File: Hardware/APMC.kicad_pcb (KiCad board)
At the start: 2 copper layers, 85 x 52.5 mm, 148 parts, among them J1 Pin header Male 2x7 P:1.27, J10 Conn_01x03, J11 Conn_01x03, J12 Conn_02x08, J13 Conn_01x03, J14 Conn_01x04, J2 USB-C receptacle, J5 Terminal 1x5 P:3.5mm, J6 Terminal 1x5 P:3.5mm, J7 Terminal 1x5 P:3.5mm, J8 Conn_01x04, J9 Conn_01x04, M1 Logo_Open_Hardware_Small, Q1 DMP6023LE, Q2 DMP6023LE, Q3 DMP6023LE, Q4 BSS123, Q5 DMP6023LE, Q6 DMP6023LE, Q7 BSS123, Q8 DMP3056L, U1 LMR51610, U10 TXU0202, U11 PCA9306, U12 LM74703/LM74704, U13 TPS62162DSG, U2 LCFE201202A, U3 TXU0202, U4 M95P32, U5 STM32U575CITx, U6 XTR200, U7 TPS7A2031PDBVR, U8 XTR200, U9 ADS1x2S14, X1 SiT8008Bx-7x, Y1 32.768kHz

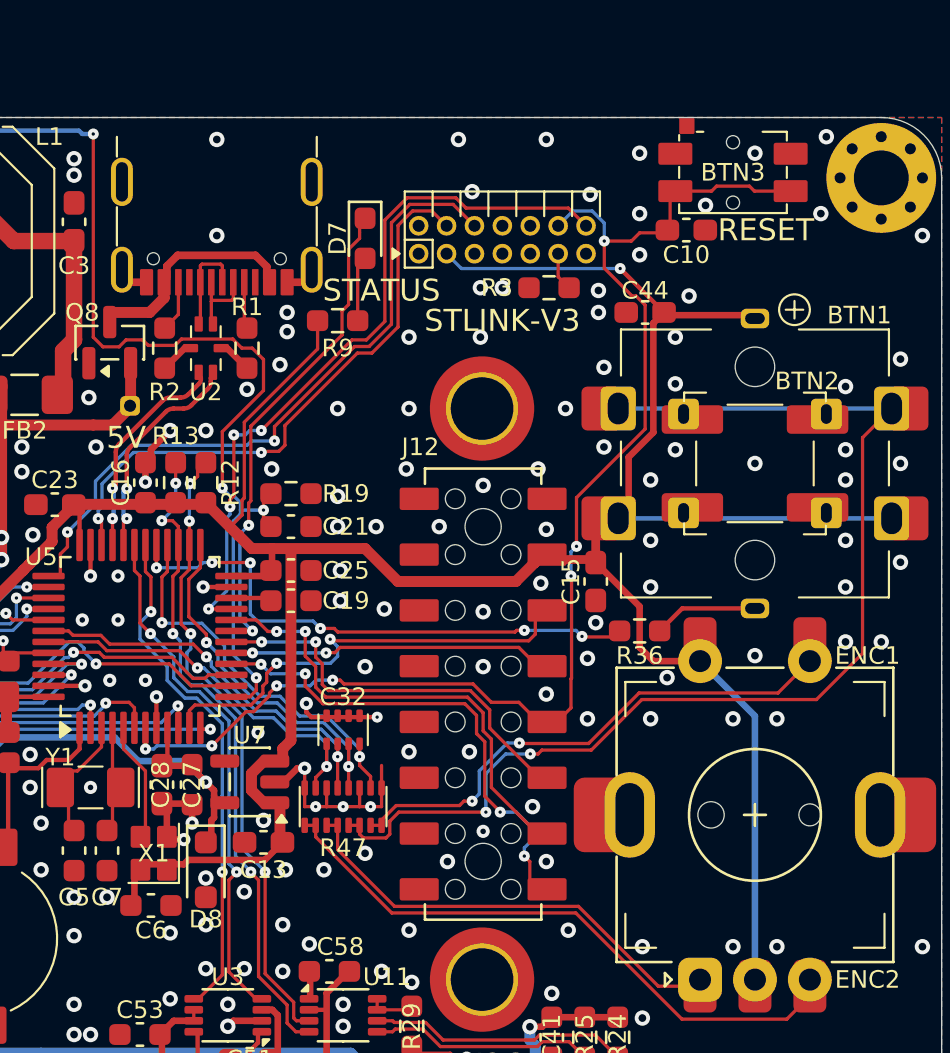
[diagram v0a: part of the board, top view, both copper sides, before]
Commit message: LCD pin header modified
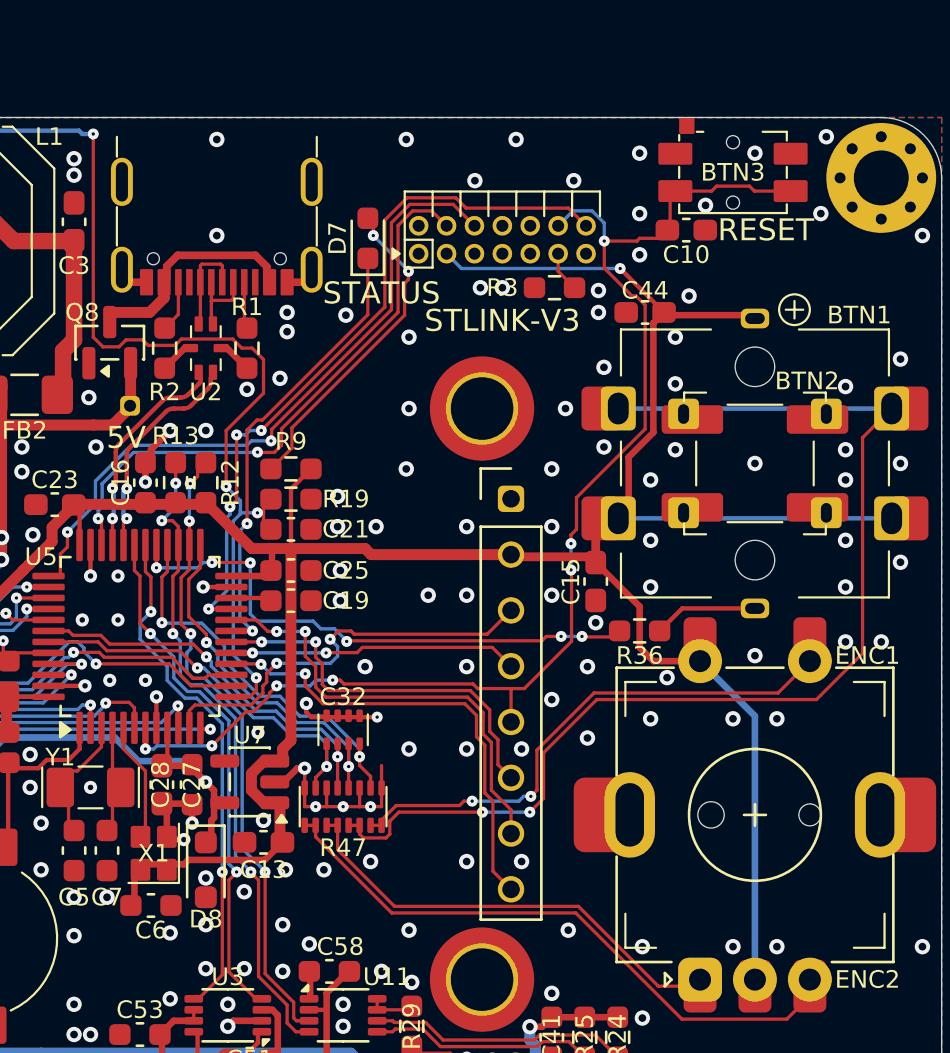
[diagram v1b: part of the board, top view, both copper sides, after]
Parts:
- J12: value Conn_02x08 -> Conn_01x08; footprint Custom:Harwin_M20-7810845_2x08_P2.54mm_Vertical -> Custom:PinHeader_1x08_P2.54mm_Vertical
- moved R9 7.08 mm to (82.9, 29.0), turned to 0 degrees
- moved J12 1.27 mm to (92.9, 39.2)
- moved R19 0.25 mm to (82.9, 30.4)
- moved R3 0.25 mm to (94.9, 20.8)
- moved C21 0.12 mm to (82.9, 31.8)
- moved D7 0.12 mm to (86.4, 18.5), turned to 90 degrees
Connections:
- J12 pad 1: unconnected-(J12-Pin_1-Pad1) -> GND
- J12 pad 2: GND -> /VDD
- J12 pad 3: unconnected-(J12-Pin_3-Pad3) -> /LCD_SCK
- J12 pad 4: /VDD -> /LCD_MOSI
- J12 pad 5: unconnected-(J12-Pin_5-Pad5) -> /NRST
- J12 pad 6: /LCD_SCK -> /LCD_DC
- J12 pad 7: unconnected-(J12-Pin_7-Pad7) -> /LCD_CS
- J12 pad 8: /LCD_MOSI -> /LCD_PWM
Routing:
- net Net-(D7-A): track 2.98 -> 14.9 mm, vias 0 -> 2
- net /VDD: track 284.5 -> 277.4 mm
- net /LCD_SCK: track 20.5 -> 18.9 mm
- net /STATUS_LED: track 22.2 -> 20.7 mm
- net /NRST: track 59.5 -> 58.4 mm
- net /LCD_PWM: track 22.0 -> 21.0 mm, vias 4 -> 2
- net /LCD_MOSI: track 14.3 -> 13.3 mm
- net /ADC0: track 63.0 -> 63.9 mm
- net GND: vias 328 -> 324

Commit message: PCB refined
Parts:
- moved R9 10.6 mm to (89.5, 20.8)
- moved BT1 4.12 mm to (72.8, 50.4)
- moved R6 3.51 mm to (68.9, 43.4)
- moved C13 3.50 mm to (85.1, 46.0)
- moved C16 3.50 mm to (79.8, 29.6)
- moved C19 3.50 mm to (86.4, 35.0)
- moved C21 3.50 mm to (86.4, 31.8)
- moved C22 3.50 mm to (72.6, 42.4)
- moved C23 3.50 mm to (75.6, 30.6)
- moved C24 3.50 mm to (72.6, 41.0)
- moved C25 3.50 mm to (86.4, 33.6)
- moved C26 3.50 mm to (72.4, 39.4)
- moved C27 3.50 mm to (80.5, 43.4)
- moved C28 3.50 mm to (81.9, 43.4)
- moved C32 3.50 mm to (88.8, 40.9)
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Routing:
- net Net-(D7-A): track 14.9 -> 4.20 mm
- net /C: track 24.3 -> 17.8 mm
- net /5V: track 104.3 -> 99.5 mm
- net /NRST: track 58.4 -> 53.8 mm
- net /A: track 20.7 -> 16.8 mm
- net /D: track 53.1 -> 49.4 mm
- net /LCD_DC: track 17.5 -> 14.0 mm
- net /LCD_PWM: track 21.0 -> 17.5 mm
- net /LCD_MOSI: track 13.3 -> 9.82 mm
- net /LCD_CS: track 20.4 -> 16.9 mm
- net /LCD_SCK: track 18.9 -> 15.4 mm
- net /PWM0: track 24.9 -> 21.7 mm
- net /EF2: track 38.7 -> 41.7 mm
- net /PWM2: track 31.9 -> 34.9 mm
- net /PWM1: track 32.4 -> 35.4 mm
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
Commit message: rev 2.1 work in progress
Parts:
- removed Q8: DMP3056L, Package_TO_SOT_SMD:SOT-23
- removed R37, R38: 10k, Resistor_SMD:R_0603_1608Metric_Pad0.98x0.95mm_HandSolder
- removed R42: 19.1k, Resistor_SMD:R_0603_1608Metric_Pad0.98x0.95mm_HandSolder
- removed R43: 100k, Resistor_SMD:R_0603_1608Metric_Pad0.98x0.95mm_HandSolder
- removed U1: LMR51610, Package_TO_SOT_SMD:SOT-23-6
- added BTN4: SW_Push, Custom:Schurter_MCS-18a, F.Cu at (103.0, 27.8)
- added C1: 1uF/10V, Custom:C_0603_1608Metric_Pad0.98x0.95mm_HandSolder, F.Cu at (73.5, 20.0)
- added C31: 1.5nF, Custom:C_0603_1608Metric_Pad0.98x0.95mm_HandSolder, F.Cu at (76.2, 23.8)
- added C34: 100nF, Custom:C_0603_1608Metric_Pad0.98x0.95mm_HandSolder, F.Cu at (84.1, 23.4)
- added C38: 1uF/10V, Custom:C_0603_1608Metric_Pad0.98x0.95mm_HandSolder, F.Cu at (54.4, 44.2)
- added C43: 1uF/10V, Custom:C_0603_1608Metric_Pad0.98x0.95mm_HandSolder, F.Cu at (60.1, 46.0)
- added C52: 100pF, Custom:0603_0805, F.Cu at (42.2, 62.8)
- added C57: 100pF, Custom:0603_0805, F.Cu at (44.2, 62.8)
- added C59: 100pF, Custom:0603_0805, F.Cu at (46.2, 62.8)
- added C60: 100pF, Custom:0603_0805, F.Cu at (48.2, 62.8)
- added D15: Red LED, Custom:LED_0603_1608Metric_Pad1.05x0.95mm_HandSolder, F.Cu at (85.6, 22.6)
- added D16: TVS 5V U, Custom:D_SOD-123F, F.Cu at (73.5, 15.8)
- added D57: SS10200HE, Custom:D_SOD-123F, F.Cu at (73.4, 25.5)
- added R16: 100k, Resistor_SMD:R_0603_1608Metric_Pad0.98x0.95mm_HandSolder, F.Cu at (61.2, 25.5)
- added R219: 330R/200mA, Resistor_SMD:R_0603_1608Metric_Pad0.98x0.95mm_HandSolder, F.Cu at (60.1, 42.8)
- added R22: 5.6k, Resistor_SMD:R_0603_1608Metric_Pad0.98x0.95mm_HandSolder, F.Cu at (81.8, 27.0)
- added R23: 680R, Resistor_SMD:R_0603_1608Metric_Pad0.98x0.95mm_HandSolder, F.Cu at (85.0, 25.6)
- added R4: 360k, Resistor_SMD:R_0603_1608Metric_Pad0.98x0.95mm_HandSolder, F.Cu at (73.4, 29.8)
- added R48: 162k, Resistor_SMD:R_0603_1608Metric_Pad0.98x0.95mm_HandSolder, F.Cu at (56.8, 48.0)
- added R49: 115k, Resistor_SMD:R_0603_1608Metric_Pad0.98x0.95mm_HandSolder, F.Cu at (56.8, 46.6)
- added R50: 115k, Resistor_SMD:R_0603_1608Metric_Pad0.98x0.95mm_HandSolder, F.Cu at (56.8, 41.9)
- added R51: 162k, Resistor_SMD:R_0603_1608Metric_Pad0.98x0.95mm_HandSolder, F.Cu at (56.8, 40.5)
- added R52: 64.9k, Resistor_SMD:R_0603_1608Metric_Pad0.98x0.95mm_HandSolder, F.Cu at (59.9, 25.5)
- added U14: OPA2387DSG, Custom:WSON-8-1EP_2x2mm_P0.5mm_EP0.9x1.6mm, F.Cu at (56.8, 44.2)
- added U15: TPS259461A, Custom:VQFN-HR-10-RPW, F.Cu at (76.1, 26.0)
- added U16: TUSB320, Package_DFN_QFN:Texas_X2QFN-12_1.6x1.6mm_P0.4mm, F.Cu at (81.8, 23.4)
- added U17: LMR38015, Custom:TI_WSON-12-1EP_3x3mm_P0.5mm_EP1.3x2.5mm_ThermalVias, F.Cu at (58.4, 21.8)
- BTN3: renamed from BTN2; footprint Custom:tactile_switch_6x6 -> Custom:tactile_switch_6x6_LED
- C13: value 1uF/4V -> 4.7uF/6.3; footprint Capacitor_SMD:C_0603_1608Metric_Pad1.08x0.95mm_HandSolder -> Custom:C_0603_1608Metric_Pad0.98x0.95mm_HandSolder
- C28: value 4.7uF/4V -> 1uF/10V
- C33: value 10nF -> 1.5nF; footprint Custom:RC_Array_Isolated_4_0805 -> Custom:C_0603_1608Metric_Pad0.98x0.95mm_HandSolder
- C45, C46: value 10nF -> 100pF
- J2: value USB-C receptacle -> USB4105-GF-A
- L1: value 33uH -> 22uH
- Q1: value DMP6023LE -> FDT86102LZ
- R1: value 5.1k -> 11R
- R11, R17: value 1k -> 1.69k
- R2: value 5.1k -> 887k
- R20, R21, R27, R28, R32, R33, R34, R35: footprint Resistor_SMD:R_0805_2012Metric -> Custom:0603_0805
- R45: value 25.5k -> 27k
- R5: value 10k -> 100k
- moved C33 43.7 mm to (75.9, 28.9)
- moved C3 16.2 mm to (57.0, 15.2), turned to 90 degrees
- moved C46 7.92 mm to (54.4, 41.0), turned to -90 degrees
- moved J4 6.91 mm to (72.1, 32.1)
- moved C45 6.06 mm to (54.4, 47.5), turned to 90 degrees
- moved R2 5.09 mm to (81.8, 25.6), turned to 0 degrees
- moved R1 4.76 mm to (76.2, 22.4), turned to 0 degrees
- moved C50 4.63 mm to (69.1, 29.5), turned to 180 degrees
- moved R40 3.56 mm to (52.9, 48.8), turned to 90 degrees
- moved Q4 3.31 mm to (57.4, 35.8)
- moved C39 3.30 mm to (58.6, 27.9), turned to 180 degrees
- moved J3 3.25 mm to (60.6, 38.1)
- moved C29 2.50 mm to (51.5, 55.9)
- moved C30 2.50 mm to (51.5, 57.6)
- moved C37 2.50 mm to (49.1, 57.1)
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- renumbered BTN3 to BTN1, BTN1 to BTN2
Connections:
- BTN2 pad 3: Net-(BTN1-K) -> Net-(BTN2-K)
- C13 pad 1: /VDD -> GND
- C13 pad 2: GND -> /VDD
- C33 pad 1: /ADC1 -> GND
- C33 pad 2: /ADC2 -> Net-(U15-DVDT)
- C45 pad 1: GND -> Net-(U14A--)
- C45 pad 2: Net-(U6-Input) -> Net-(U8-Input)
- C46 pad 1: GND -> Net-(U14B--)
- C46 pad 2: Net-(U8-Input) -> Net-(U6-Input)
- ENC2 pad B: /B -> unconnected-(ENC2-PadB)
- J2 pad A8: unconnected-(J2-SBU1-PadA8) -> (no net)
- J2 pad B8: unconnected-(J2-SBU2-PadB8) -> (no net)
- R1 pad 1: GND -> Net-(D57-A)
- R1 pad 2: /CC1 -> /USB_VBUS
- R2 pad 1: GND -> /USB_VBUS
- R2 pad 2: /CC2 -> Net-(U16-VBUS_DET)
- R36 pad 1: Net-(BTN1-K) -> Net-(BTN2-K)
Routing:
- net /PG5: track 0.00 -> 30.2 mm, vias 0 -> 4
- net /VDD: track 275.7 -> 296.3 mm, vias 7 -> 11
- net /USB_VBUS: track 9.52 -> 22.0 mm, vias 0 -> 2
- net Net-(U15-~{FLT}): track 0.00 -> 11.1 mm, vias 0 -> 2
- net /5V: track 99.5 -> 110.2 mm, vias 2 -> 1
- net Net-(BTN2-K): track 0.00 -> 10.0 mm
- net Net-(U17-FB): track 23.8 -> 33.0 mm, vias 0 -> 2
- net Net-(U14C-V+): track 0.00 -> 6.42 mm, vias 0 -> 2
- net /ADC1: track 13.7 -> 20.1 mm, vias 0 -> 2
- net Net-(U15-EN/UVLO): track 0.00 -> 6.26 mm, vias 0 -> 2
- net Net-(U1-FB): track 5.67 -> 0.00 mm, vias 2 -> 0
- net Net-(U16-VBUS_DET): track 0.00 -> 5.61 mm, vias 0 -> 2
- net Net-(U14A--): track 0.00 -> 5.56 mm
- net Net-(U14B--): track 0.00 -> 5.53 mm
- net /I2C_SCL: track 29.1 -> 33.9 mm
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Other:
- board text added: "All-purpose Micro Controller (APMC) rev. 2.1 2026-08-02"
- board text added: "Copyright © 2026 Tomasz Jastrzębski"
- board text removed: "All-purpose Micro Controller (APMC) rev. 2.0.1 2026-07-21"

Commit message: refinement
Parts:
- moved L2 7.20 mm to (61.1, 31.8), turned to -90 degrees
- moved R46 6.23 mm to (55.6, 15.2), turned to 90 degrees
- moved D4 5.97 mm to (68.5, 33.5)
- moved C50 4.78 mm to (65.9, 33.0), turned to 90 degrees
- moved C49 4.64 mm to (68.8, 28.0), turned to 90 degrees
- moved C39 3.54 mm to (61.2, 25.5), turned to 90 degrees
- moved R16 2.40 mm to (63.6, 25.9), turned to 180 degrees
- moved FB2 2.39 mm to (71.1, 28.0), turned to 90 degrees
- moved J4 2.24 mm to (70.1, 31.1)
- moved BT1 1.29 mm to (71.6, 51.0)
- moved U13 0.75 mm to (66.1, 29.2), turned to 180 degrees
- moved C22 0.62 mm to (73.4, 43.0)
- moved C12 0.25 mm to (52.8, 14.5)
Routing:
- net /ADC0: track 67.4 -> 61.9 mm
- net GND: track 94.0 -> 90.7 mm, vias 321 -> 333
- net /VIN: track 32.7 -> 35.7 mm
- net /5V: track 110.2 -> 107.7 mm
- net /VDD: track 296.3 -> 298.3 mm
- net /VBAT: track 5.73 -> 7.66 mm
- net Net-(U17-EN): track 8.47 -> 10.3 mm
- net /PG5: track 30.2 -> 28.6 mm, vias 4 -> 6
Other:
- board text added: "All-purpose Micro Controller (APMC) rev. 2.1 2026-08-22"
- board text removed: "All-purpose Micro Controller (APMC) rev. 2.1 2026-08-02"

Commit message: refinement
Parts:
- H1, H2, H3, H4: value M2.5x7 -> M2.5x6
- H10, H11, H12, H13: value Standoff_M2x4.0 -> Standoff_M2x3.0
- J1: footprint Custom:PinHeader_2x07_P1.27mm_Horizontal-UP -> Custom:PinHeader_2x07_P1.27mm_Horizontal-UP-0.15
- moved M1 4.44 mm to (52.1, 61.0)
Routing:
- net /VDD: track 298.3 -> 297.4 mm
- net GND: vias 333 -> 335
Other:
- board text added: "All-purpose Micro Controller (APMC) rev. 2.1 2026-08-23"
- board text removed: "All-purpose Micro Controller (APMC) rev. 2.1 2026-08-22"
